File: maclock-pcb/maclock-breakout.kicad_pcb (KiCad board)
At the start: 2 copper layers, 70.5 x 26.5 mm, 11 parts, among them J1 B2B-ZR(LF)(SN), J2 B4B-ZR(LF)(SN), SW1 TSB001A3518A, SW2 TSB001A3518A

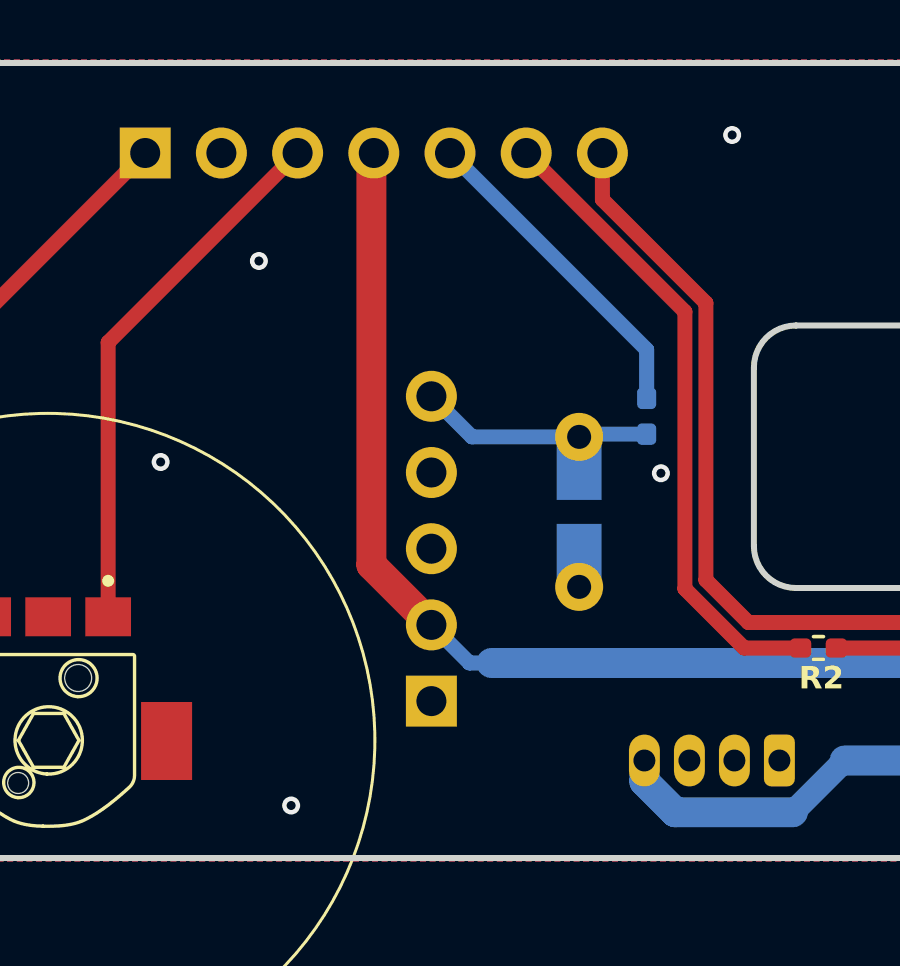
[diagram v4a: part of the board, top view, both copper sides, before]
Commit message: PCB rev 2: on-board PAM8302A amp replaces the Adafruit module
- U1 PAM8302AASCR (C113367) on the bottom side where the JP1 socket was; JP1 removed
- Input: A+ -> C2 220n -> R4 47k -> IN+; IN- via R5 47k + C3 220n to GND (gain ~9 dB)
- C4 1u + C5 10u decoupling, fed by via from the F.Cu 5V trunk; new 5V via at the old
  JP1 pin-2 spot keeps the F.Cu/B.Cu 5V runs joined
- SD pulled up by R6 100k; also brought out on a new PiInput pin 8 (MUTE) along the
  top edge, so the header is now 1x8 (C492407)
- J3 JST ZH 2P speaker connector (C158011), + / - silk, pad 1 = SPK+
- Schematic: new parts + nets, PWR_FLAGs on 5V/GND; ERC 0/0. DRC 0 errors, 0 unconnected,
  parity only benign field/NC notes. scripts/add_onboard_amp.py rebuilds it from 5ece6d9
- Docs: PCB README BOM + amp section, PCBway reply, build-guide wiring table, root README
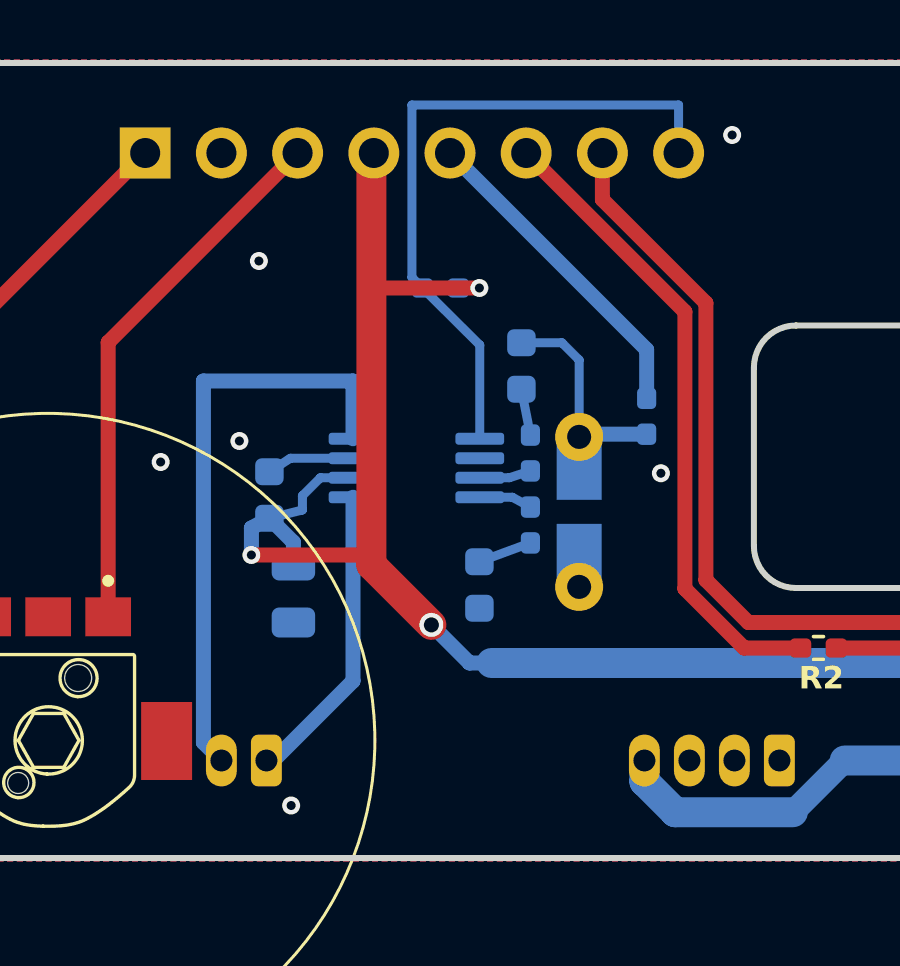
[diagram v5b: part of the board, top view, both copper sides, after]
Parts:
- removed JP1: 2.54-1*5PFemale, Connector_PinSocket_2.54mm:PinSocket_1x05_P2.54mm_Vertical
- removed the PiInput at (129.5, 81.0)
- added C2: 220nF, Capacitor_SMD:C_0603_1608Metric, B.Cu at (142.0, 88.1)
- added C3: 220nF, Capacitor_SMD:C_0603_1608Metric, B.Cu at (140.6, 95.4)
- added C4: 1uF, Capacitor_SMD:C_0603_1608Metric, B.Cu at (133.6, 92.4)
- added C5: 10uF, Capacitor_SMD:C_0805_2012Metric, B.Cu at (134.4, 95.7)
- added J3: B2B-ZR(LF)(SN), Connector_JST:JST_ZH_B2B-ZR_1x02_P1.50mm_Vertical, B.Cu at (133.5, 101.2)
- added PiInput: PZ254V-11-08P, Connector_PinHeader_2.54mm:PinHeader_1x08_P2.54mm_Vertical, B.Cu at (129.5, 81.0)
- added R4: 47K, Resistor_SMD:R_0402_1005Metric_Pad0.72x0.64mm_HandSolder, B.Cu at (142.3, 91.0)
- added R5: 47K, Resistor_SMD:R_0402_1005Metric_Pad0.72x0.64mm_HandSolder, B.Cu at (142.3, 93.4)
- added R6: 100K, Resistor_SMD:R_0402_1005Metric_Pad0.72x0.64mm_HandSolder, B.Cu at (139.3, 85.5)
- added U1: PAM8302AASCR, Package_SO:MSOP-8_3x3mm_P0.65mm, B.Cu at (138.5, 91.5)
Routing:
- net /AMP_SD: track 0.00 -> 22.6 mm
- net /SPK-: track 0.00 -> 19.8 mm
- net /5V: track 46.1 -> 61.4 mm, vias 0 -> 3
- net /SPK+: track 0.00 -> 10.1 mm
- net /GND: track 0.00 -> 2.92 mm, vias 13 -> 14
- net Net-(C3-Pad2): track 0.00 -> 1.81 mm
- net Net-(U1-IN-): track 0.00 -> 1.77 mm
- net Net-(U1-IN+): track 0.00 -> 1.72 mm
- net Net-(C2-Pad2): track 0.00 -> 1.56 mm
- net /A+: track 7.77 -> 7.01 mm
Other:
- board text added: "MUTE"
- board text removed: "Adafruit PAM8302"

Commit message: C1: plain 0603 land (10nF X7R, C57112) replaces the chip-or-disc hybrid
- All passives are SMD now; the hybrid THT/SMD land and its library footprint are gone
- C1 sits vertically at (143.925, 92.96) on B.Cu, A+ on top toward R3, GND below to the pour
- scripts/c1_plain_0603.py replays it from 5d96fa9; ERC 0, DRC 0 errors / 0 unconnected
- README BOM, sourcing table and PCBway reply updated; the 'chip or disc' section removed
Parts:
- C1: footprint maclock:C_Chip_or_Disc_P5mm_SMD -> Capacitor_SMD:C_0603_1608Metric
- moved C1 2.50 mm to (143.9, 93.0)
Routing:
- net /A+: track 7.01 -> 8.74 mm

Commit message: Drop the MUTE header pin; PiInput back to 1x7
pinctrl on the running Maclock shows the Waveshare DPI overlay owns GPIO 0-9, 12-17, 20-25 and
10/11/18/19/26/27 are the dial, backlight, audio and buttons, so no header GPIO can drive the
amp's shutdown pin. R6 keeps it high (amp always on); the top-edge SD run, pad 8 and the MUTE
silk are removed. scripts/revert_mute_pin.py replays it from 1f01ab1. ERC 0, DRC 0/0.
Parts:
- removed the PiInput at (129.5, 81.0)
- added PiInput: PZ254V-11-07P, Connector_PinHeader_2.54mm:PinHeader_1x07_P2.54mm_Vertical, B.Cu at (129.5, 81.0)
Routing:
- net /AMP_SD: track 22.6 -> 5.82 mm
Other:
- board text removed: "MUTE"

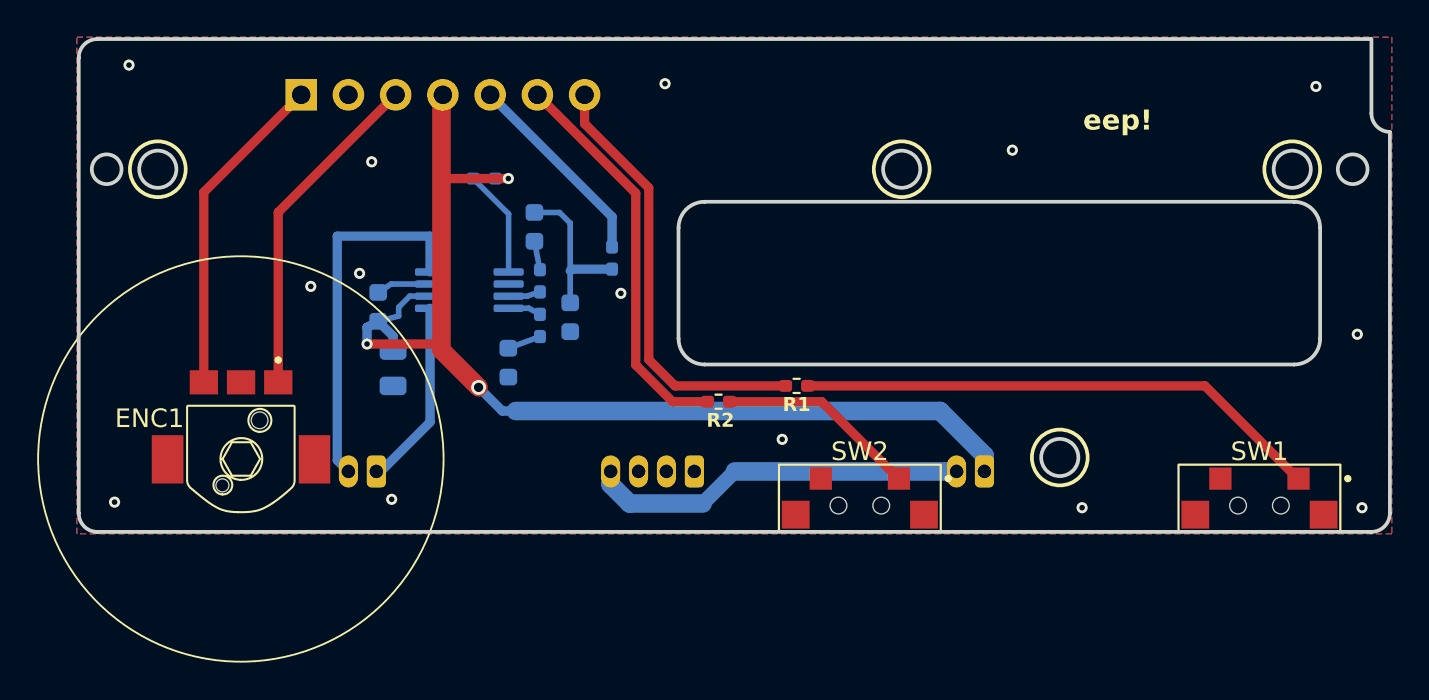
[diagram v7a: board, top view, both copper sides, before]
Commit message: PCB: compact amp block beside the Pi header, R3/C1 next to U1, 5V via ring 0.25 mm
Hand layout pass: the amp, its passives and the R3/C1 filter now sit in a tight grid at
x 127-137 next to the Pi header, U1 inputs facing the passives and outputs facing J3 at
(137.75, 101.25). All pad-to-net assignments unchanged. The 5V trunk via was 1.0/0.73
(0.135 mm ring, under PCBway's 0.15 mm); now 1.0/0.5. DRC 0 errors / 0 unconnected.
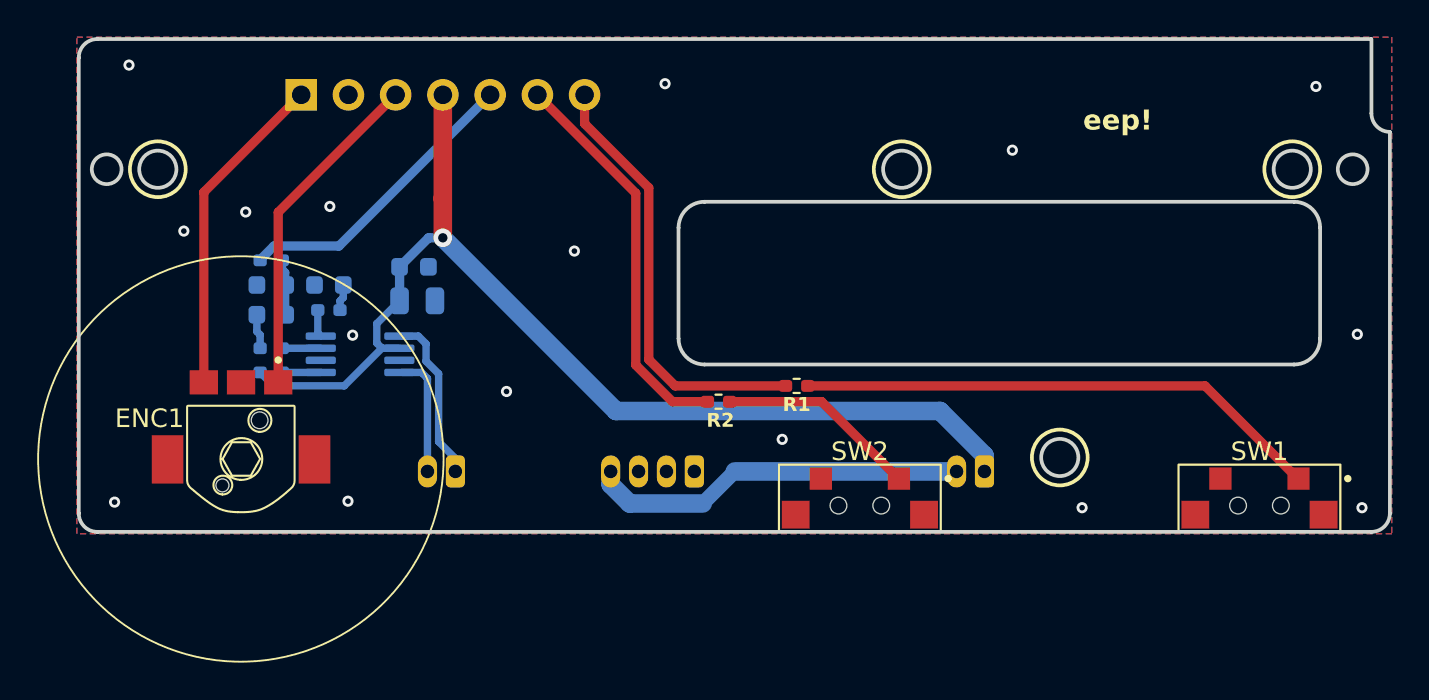
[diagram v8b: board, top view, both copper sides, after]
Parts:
- moved R3 18.3 mm to (127.8, 89.9), turned to 0 degrees
- moved C1 16.2 mm to (127.8, 91.2), turned to 0 degrees
- moved R6 15.5 mm to (127.8, 95.9), turned to 0 degrees
- moved C2 14.9 mm to (127.8, 92.8), turned to 180 degrees
- moved R4 14.9 mm to (127.8, 94.6), turned to 0 degrees
- moved R5 11.4 mm to (130.9, 92.6), turned to 180 degrees
- moved C3 10.5 mm to (130.9, 91.2), turned to 0 degrees
- moved U1 6.81 mm to (132.6, 95.0), turned to 0 degrees
- moved J3 4.25 mm to (137.8, 101.2)
- moved C5 3.85 mm to (135.7, 92.1), turned to 0 degrees
- moved C4 2.89 mm to (135.5, 90.2), turned to 0 degrees
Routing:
- net /SPK-: track 19.8 -> 6.50 mm
- net /A+: track 8.74 -> 3.00 mm
- net /AUDIO: track 10.9 -> 16.0 mm
- net /AMP_SD: track 5.82 -> 2.06 mm
- net /GND: track 2.92 -> 0.00 mm, vias 14 -> 16
- net /5V: track 61.4 -> 59.1 mm, vias 3 -> 1
- net /SPK+: track 10.1 -> 8.97 mm
